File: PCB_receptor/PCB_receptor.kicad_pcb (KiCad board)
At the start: 2 copper layers, 120.6 x 96.3 mm, 6 parts, among them J1 Screw_Terminal_01x02

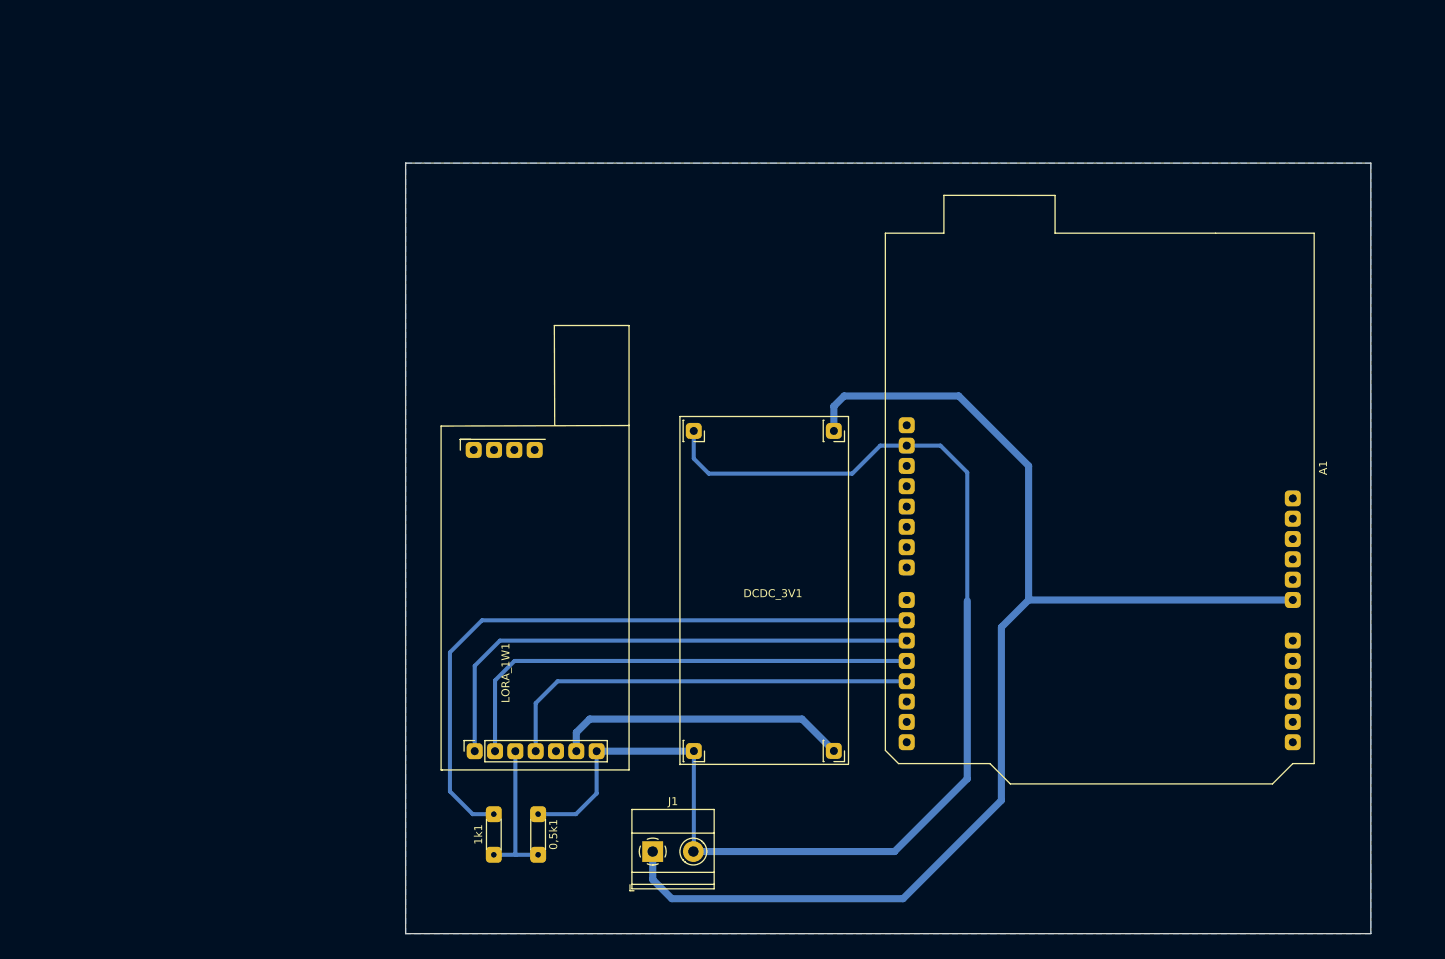
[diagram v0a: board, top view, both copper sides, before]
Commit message: Adicionado furos de fixação
Adicionado furos de fixação
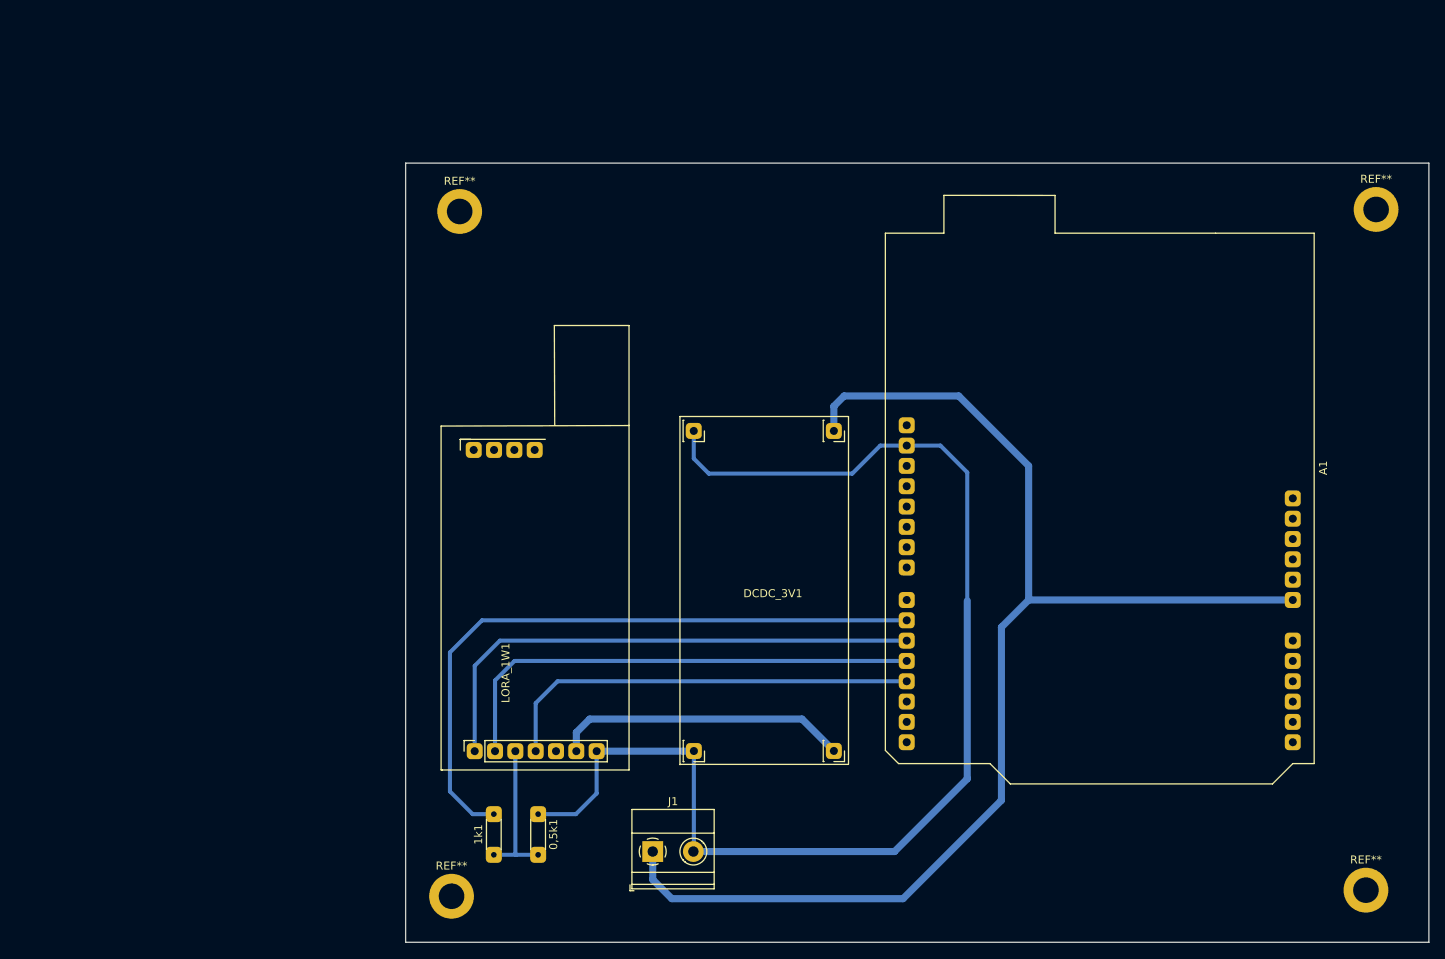
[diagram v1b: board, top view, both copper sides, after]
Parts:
- added REF**: MountingHole_3.2mm_M3_DIN965_Pad, MountingHole:MountingHole_3.2mm_M3_DIN965_Pad, F.Cu at (218.7, 136.1)
- added REF**: MountingHole_3.2mm_M3_DIN965_Pad, MountingHole:MountingHole_3.2mm_M3_DIN965_Pad, F.Cu at (220.0, 51.1)
- added REF**: MountingHole_3.2mm_M3_DIN965_Pad, MountingHole:MountingHole_3.2mm_M3_DIN965_Pad, F.Cu at (105.4, 51.3)
- added REF**: MountingHole_3.2mm_M3_DIN965_Pad, MountingHole:MountingHole_3.2mm_M3_DIN965_Pad, F.Cu at (104.4, 136.9)
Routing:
- removed copper zone on B.Cu, net GND
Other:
- board size 120.6 x 96.3 mm -> 127.9 x 97.4 mm

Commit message: Placa do Receptor atualizada
Adicionados:
LED's indicativos
Capacitores para solucinonar defeito de fábrica da Shield Ethernet
Resistores para divisor de tensão e Pull-Up
Disposição dos componentes na placa refeito
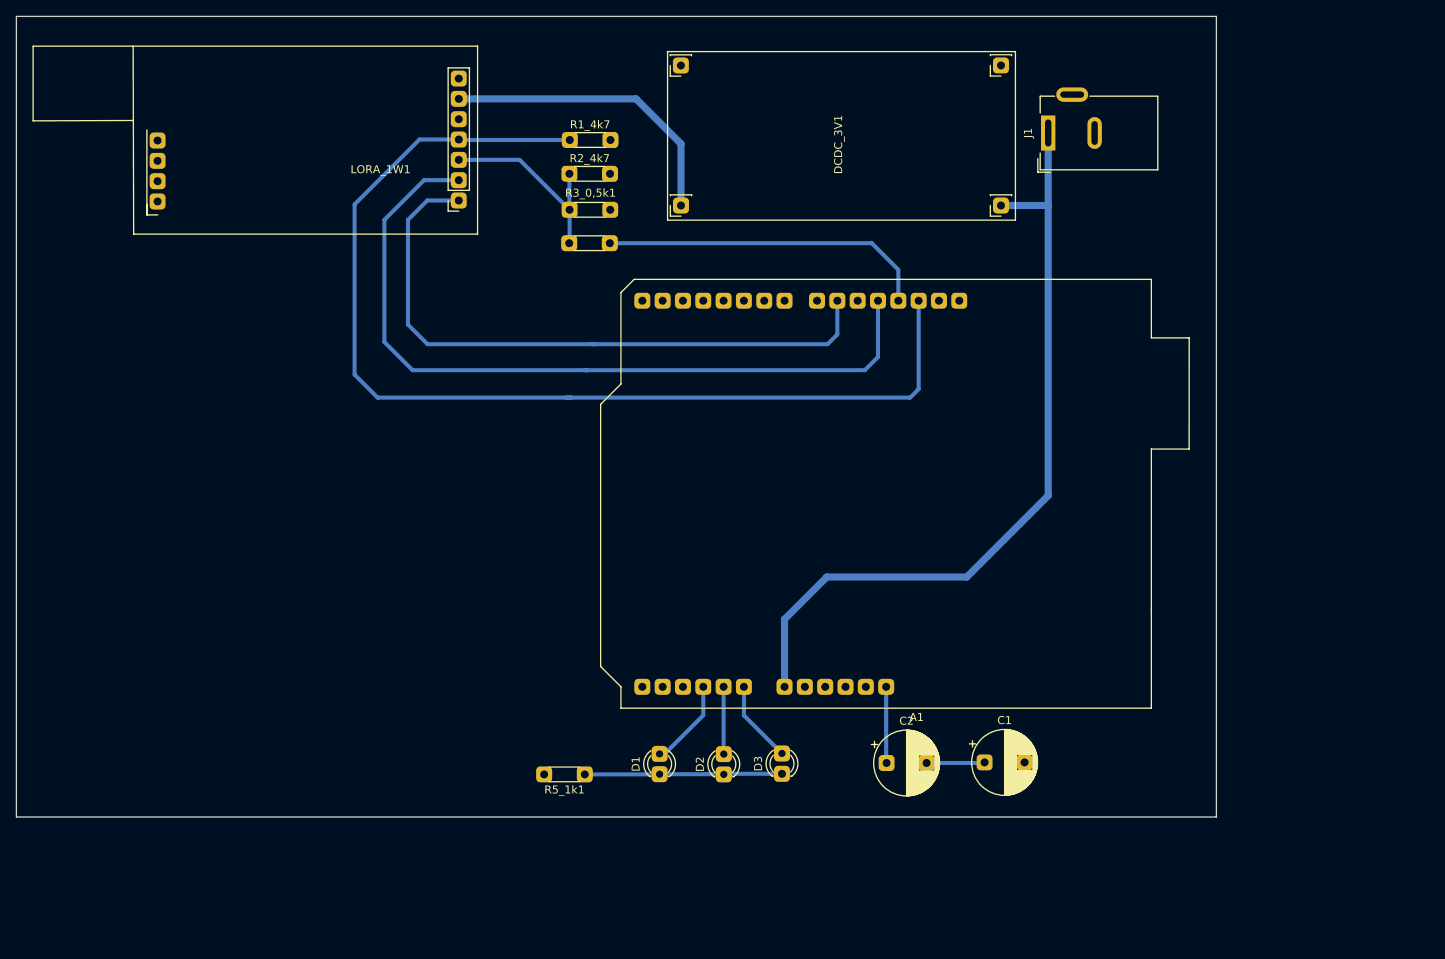
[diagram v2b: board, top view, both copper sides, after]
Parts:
- removed 0,5k1: R, Resistor_THT:R_Axial_DIN0204_L3.6mm_D1.6mm_P5.08mm_Horizontal
- removed REF** (x4): MountingHole_3.2mm_M3_DIN965_Pad, MountingHole:MountingHole_3.2mm_M3_DIN965_Pad
- added C1: CP, Capacitor_THT:CP_Radial_D8.0mm_P5.00mm, F.Cu at (171.0, 120.2)
- added C2: CP, Capacitor_THT:CP_Radial_D8.0mm_P5.00mm, F.Cu at (158.8, 120.2)
- added D1: LED, LED_THT:LED_D3.0mm, F.Cu at (130.4, 121.7)
- added D2: LED, LED_THT:LED_D3.0mm, F.Cu at (138.4, 121.7)
- added D3: LED, LED_THT:LED_D3.0mm, F.Cu at (145.7, 121.6)
- added R1_4k7: R1, Resistor_THT:R_Axial_DIN0204_L3.6mm_D1.6mm_P5.08mm_Horizontal, F.Cu at (119.2, 42.4)
- added R2_4k7: R2, Resistor_THT:R_Axial_DIN0204_L3.6mm_D1.6mm_P5.08mm_Horizontal, F.Cu at (119.1, 46.6)
- added R3_0,5k1: R, Resistor_THT:R_Axial_DIN0204_L3.6mm_D1.6mm_P5.08mm_Horizontal, F.Cu at (124.2, 51.1)
- added R5_1k1: R2, Resistor_THT:R_Axial_DIN0204_L3.6mm_D1.6mm_P5.08mm_Horizontal, F.Cu at (121.0, 121.7)
- 1k1: value R -> R4_1k
- A1: value Board_Ethernet_Shield_W5100 -> Board_Ethernet_Shield_W5100-Arduino_Mega
- J1: value Screw_Terminal_01x02 -> Barrel_Jack_MountingPin; footprint TerminalBlock_Phoenix:TerminalBlock_Phoenix_MKDS-1,5-2-5.08_1x02_P5.08mm_Horizontal -> Connector_BarrelJack:BarrelJack_Wuerth_6941xx301002
- moved J1 102.5 mm to (179.0, 41.5), turned to 90 degrees
- moved 1k1 77.0 mm to (119.1, 55.3), turned to 0 degrees
- moved LORA_1W1 68.9 mm to (105.3, 49.9), turned to 180 degrees
- moved DCDC_3V1 59.7 mm to (173.1, 33.0), turned to 180 degrees
- moved A1 54.0 mm to (163.8, 110.7), turned to 180 degrees
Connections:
- A1 pad 10: Net-(1k1-Pad2) -> Net-(A1-Pad10)
- A1 pad 11: M0 -> Net-(A1-Pad11)
- A1 pad 12: M1 -> Net-(A1-Pad12)
- A1 pad 13: TX_LORA -> Net-(A1-Pad13)
- A1 pad 17: Net-(A1-Pad17) -> RST
- A1 pad 23: Net-(A1-Pad23) -> A0
- A1 pad 24: Net-(A1-Pad24) -> A1
- A1 pad 25: Net-(A1-Pad25) -> A2
- A1 pad 3: Net-(A1-Pad3) -> TX_LORA
- A1 pad 4: Net-(A1-Pad4) -> Net-(1k1-Pad2)
- A1 pad 5: Net-(A1-Pad5) -> M1
- A1 pad 7: Net-(A1-Pad7) -> M0
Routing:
- net GND: track 156.0 -> 0.00 mm
- net TX_LORA: track 53.5 -> 135.3 mm
- net VIN: track 161.0 -> 99.0 mm
- net Net-(1k1-Pad2): track 82.8 -> 41.3 mm
- net M1: track 61.3 -> 97.8 mm
- net GND_LED: track 0.00 -> 24.8 mm
- net M0: track 66.0 -> 80.4 mm
- net A2: track 0.00 -> 11.8 mm
- net A0: track 0.00 -> 10.3 mm
- net RST: track 0.00 -> 9.55 mm
- net A1: track 0.00 -> 8.42 mm
- net Net-(C1-Pad1): track 0.00 -> 7.28 mm
- net RX_LORA: track 18.5 -> 25.2 mm
- net 3.3V_DCDC: track 36.9 -> 37.8 mm
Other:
- board size 127.9 x 97.4 mm -> 150 x 100.1 mm

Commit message: Atualização placa do receptor
Up
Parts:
- removed DCDC_3V1: DCDC_CHINA, Converter_DCDC:STEPDOWN_CHINA
- added STEPDOWN1: Converter_DCDC_STEPDOWN, Converter_DCDC:STEPDOWN_XL4005, F.Cu at (195.6, 46.1)
- C1, C2: value CP -> 0,1uF
- R1: renamed from R1_4k7; value R1 -> 4K7
- R2: renamed from R2_4k7; value R2 -> 4K7
- R5: renamed from R5_1k1; value R2 -> 100
- moved J1 28.5 mm to (203.8, 55.4)
- moved D3 24.7 mm to (166.0, 135.6)
- moved R5 24.7 mm to (141.4, 135.6)
- moved LORA_1W1 24.7 mm to (125.6, 63.9)
- moved R1 24.7 mm to (139.5, 56.3)
- moved 1k1 24.7 mm to (139.4, 69.2)
- moved C1 24.7 mm to (191.3, 134.1)
- moved D2 24.7 mm to (158.7, 135.6)
- moved R3_0,5k1 24.7 mm to (144.6, 65.1)
- moved A1 24.7 mm to (184.1, 124.7)
- moved C2 24.7 mm to (179.1, 134.2)
- moved D1 24.7 mm to (150.7, 135.6)
- moved R2 24.7 mm to (139.4, 60.6)
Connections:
- A1 pad 10: Net-(A1-Pad10) -> M1
- A1 pad 11: Net-(A1-Pad11) -> M0
- A1 pad 13: Net-(A1-Pad13) -> Net-(1k1-Pad2)
- A1 pad 25: A2 -> Net-(A1-Pad25)
- A1 pad 26: Net-(A1-Pad26) -> A3
- A1 pad 3: TX_LORA -> Net-(A1-Pad3)
- A1 pad 4: Net-(1k1-Pad2) -> TX_LORA
- A1 pad 5: M1 -> Net-(A1-Pad5)
- A1 pad 7: M0 -> Net-(A1-Pad7)
- D1 pad 2: A2 -> A3
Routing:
- net M0: track 80.4 -> 53.7 mm
- net Net-(1k1-Pad2): track 41.3 -> 16.0 mm
- net M1: track 97.8 -> 77.7 mm
- net A2: track 11.8 -> 0.00 mm
- net A3: track 0.00 -> 11.0 mm
- net TX_LORA: track 135.3 -> 126.5 mm
- net VIN: track 99.0 -> 93.2 mm
- net 3.3V_DCDC: track 37.8 -> 38.6 mm
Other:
- board size 150 x 100.1 mm -> 135 x 100.1 mm

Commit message: PCB Receptores Atualização
Up
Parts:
- moved A1 2.85 mm to (186.7, 123.4)
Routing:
- net RX_LORA: track 25.2 -> 30.0 mm
- net TX_LORA: track 126.5 -> 122.5 mm
- net Net-(1k1-Pad2): track 16.0 -> 18.9 mm
- net RST: track 9.55 -> 11.9 mm
- net A1: track 8.42 -> 10.8 mm
- net A3: track 11.0 -> 13.4 mm
- net M0: track 53.7 -> 55.1 mm
- net M1: track 77.7 -> 76.7 mm
- net VIN: track 93.2 -> 94.2 mm
- added copper zone on B.Cu, net GND
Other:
- board size 135 x 100.1 mm -> 136.2 x 98.9 mm
